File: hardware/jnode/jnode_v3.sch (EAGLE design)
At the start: 62 parts, among them SW1 SONDER_H_VIBRATIONSSCHALTER, U1 MPL115A, U2 L3G4200D, X1 USB-MICROB, X2 53261-03

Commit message: fix value of I2C pull-ups
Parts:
- R18, R19: value 10k -> 3.3k
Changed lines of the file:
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@@
 <attribute name="DIGIKEY" value="http://search.digikey.com/scripts/DkSearch/dksus.dll?Detail&amp;name=ATMEGA32U4-MU-ND"/>
 </part>
-<part name="R18" library="sparkfun" deviceset="RESISTOR" device="0402-RES" value="10k">
+<part name="R18" library="sparkfun" deviceset="RESISTOR" device="0402-RES" value="3.3k">
 <attribute name="DIGIKEY" value="http://search.digikey.com/scripts/DkSearch/dksus.dll?Detail&amp;name=541-2.20MLCT-ND"/>
 <attribute name="FARNELL" value="http://de.farnell.com/bourns/cr0603-jw-103elf/widerstand-0603-10k-5-0-1w/dp/2008360"/>
@@
 <part name="P+18" library="supply1" deviceset="VCC" device=""/>
 <part name="P+19" library="supply1" deviceset="VCC" device=""/>
-<part name="R19" library="sparkfun" deviceset="RESISTOR" device="0402-RES" value="10k">
+<part name="R19" library="sparkfun" deviceset="RESISTOR" device="0402-RES" value="3.3k">
 <attribute name="DIGIKEY" value="http://search.digikey.com/scripts/DkSearch/dksus.dll?Detail&amp;name=541-2.20MLCT-ND"/>
 <attribute name="FARNELL" value="http://de.farnell.com/bourns/cr0603-jw-103elf/widerstand-0603-10k-5-0-1w/dp/2008360"/>

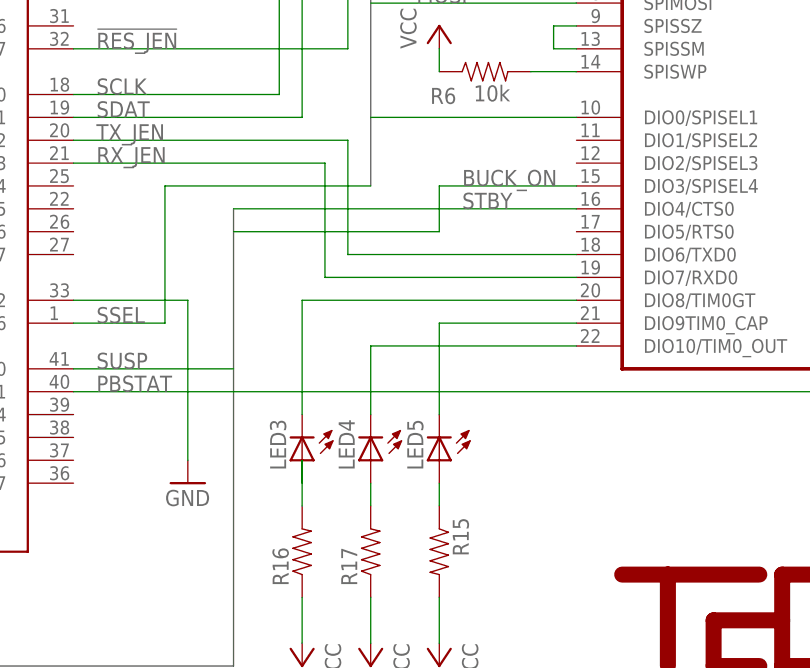
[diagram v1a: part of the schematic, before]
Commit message: Add the basic jnode-lufa firmware
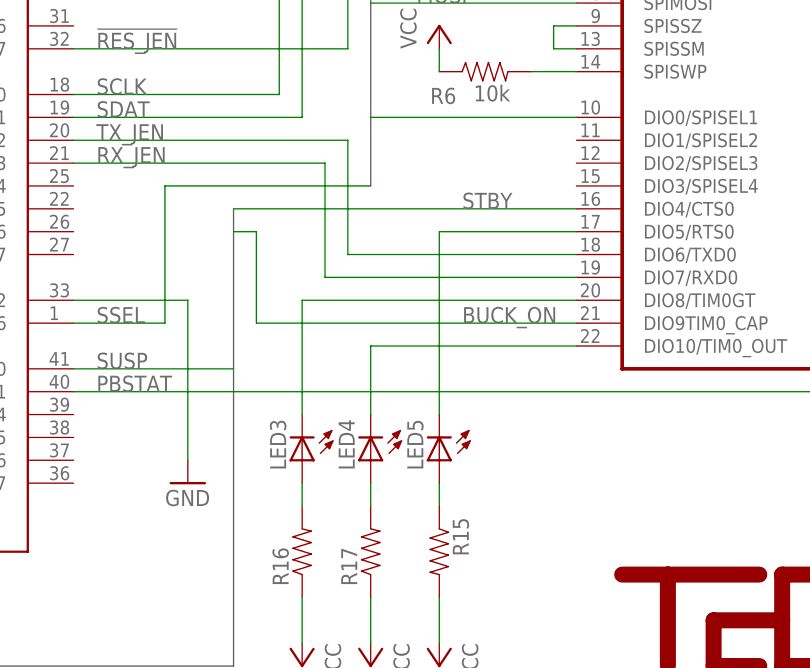
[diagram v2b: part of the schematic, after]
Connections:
- removed net N$30: LED5.C, U$1.DIO9TIM0_CAP
- new net N$7: LED5.C, U$1.DIO5/RTS0
- net BUCK_ON: now also U$1.DIO9TIM0_CAP; no longer U$1.DIO3/SPISEL4
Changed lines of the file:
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@@
 </segment>
 </bus>
-<bus name="I2C:SCLK,SDAT,TCAP,INT1">
+<bus name="I2C:SCLK,SDAT,TCAP,INT1,3G_INT2">
 <segment>
 <wire x1="375.92" y1="48.26" x2="375.92" y2="248.92" width="0.762" layer="92"/>
@@
 </segment>
 <segment>
-<wire x1="256.54" y1="58.42" x2="279.4" y2="58.42" width="0.1524" layer="91"/>
-<wire x1="279.4" y1="58.42" x2="279.4" y2="63.5" width="0.1524" layer="91"/>
-<pinref part="U$1" gate="G$1" pin="DIO3/SPISEL4"/>
-<wire x1="279.4" y1="63.5" x2="294.64" y2="63.5" width="0.1524" layer="91"/>
-<label x="281.94" y="63.5" size="1.778" layer="95"/>
+<wire x1="256.54" y1="58.42" x2="259.08" y2="58.42" width="0.1524" layer="91"/>
+<label x="281.94" y="48.26" size="1.778" layer="95"/>
+<wire x1="259.08" y1="58.42" x2="259.08" y2="48.26" width="0.1524" layer="91"/>
+<pinref part="U$1" gate="G$1" pin="DIO9TIM0_CAP"/>
+<wire x1="259.08" y1="48.26" x2="294.64" y2="48.26" width="0.1524" layer="91"/>
 </segment>
 </net>
@@
 </segment>
 </net>
-<net name="N$30" class="0">
-<segment>
-<wire x1="279.4" y1="38.1" x2="279.4" y2="48.26" width="0.1524" layer="91"/>
-<wire x1="279.4" y1="48.26" x2="294.64" y2="48.26" width="0.1524" layer="91"/>
-<pinref part="LED5" gate="G$1" pin="C"/>
-<pinref part="U$1" gate="G$1" pin="DIO9TIM0_CAP"/>
-</segment>
-</net>
 <net name="N$31" class="0">
 <segment>
@@
 <net name="N$32" class="0">
 <segment>
-<wire x1="264.16" y1="30.48" x2="264.16" y2="33.02" width="0.1524" layer="91"/>
-<wire x1="264.16" y1="33.02" x2="264.16" y2="27.94" width="0.1524" layer="91"/>
+<wire x1="264.16" y1="30.48" x2="264.16" y2="27.94" width="0.1524" layer="91"/>
 <pinref part="R16" gate="G$1" pin="2"/>
 <pinref part="LED3" gate="G$1" pin="A"/>
@@
 </segment>
 </net>
+<net name="N$7" class="0">
+<segment>
+<pinref part="LED5" gate="G$1" pin="C"/>
+<pinref part="U$1" gate="G$1" pin="DIO5/RTS0"/>
+<wire x1="279.4" y1="38.1" x2="279.4" y2="58.42" width="0.1524" layer="91"/>
+<wire x1="279.4" y1="58.42" x2="294.64" y2="58.42" width="0.1524" layer="91"/>
+</segment>
+</net>
